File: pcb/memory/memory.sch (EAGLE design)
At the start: 8 parts, among them IC1 CY62256LL-PXC, IC2 CY62256LL-PXC, IC3 74HC04D

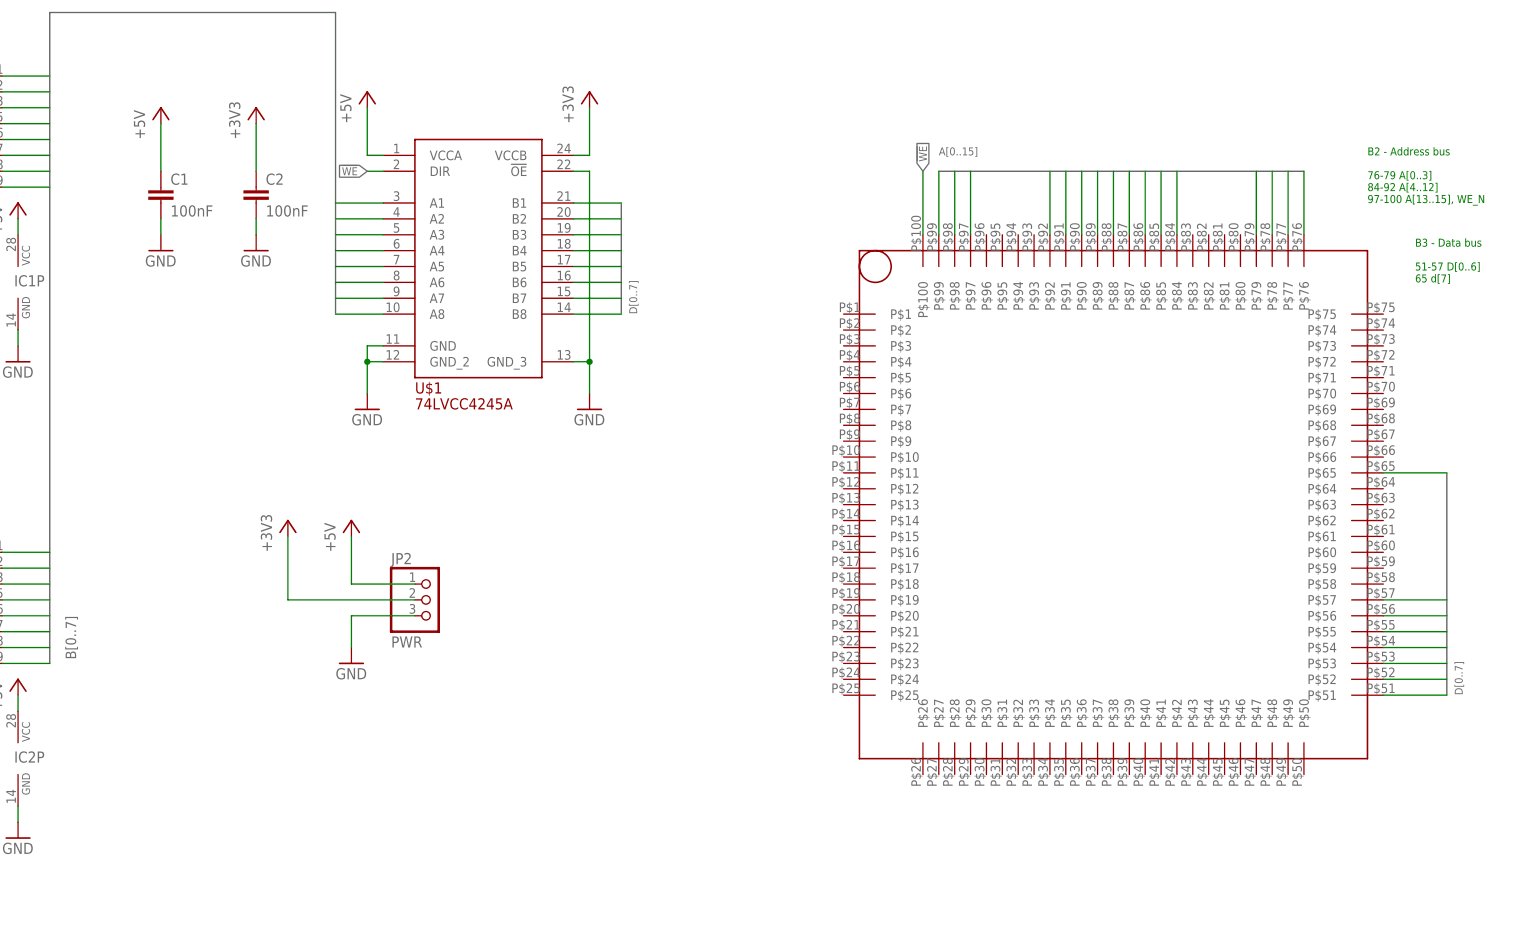
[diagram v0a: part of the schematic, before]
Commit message: Memory board with headers
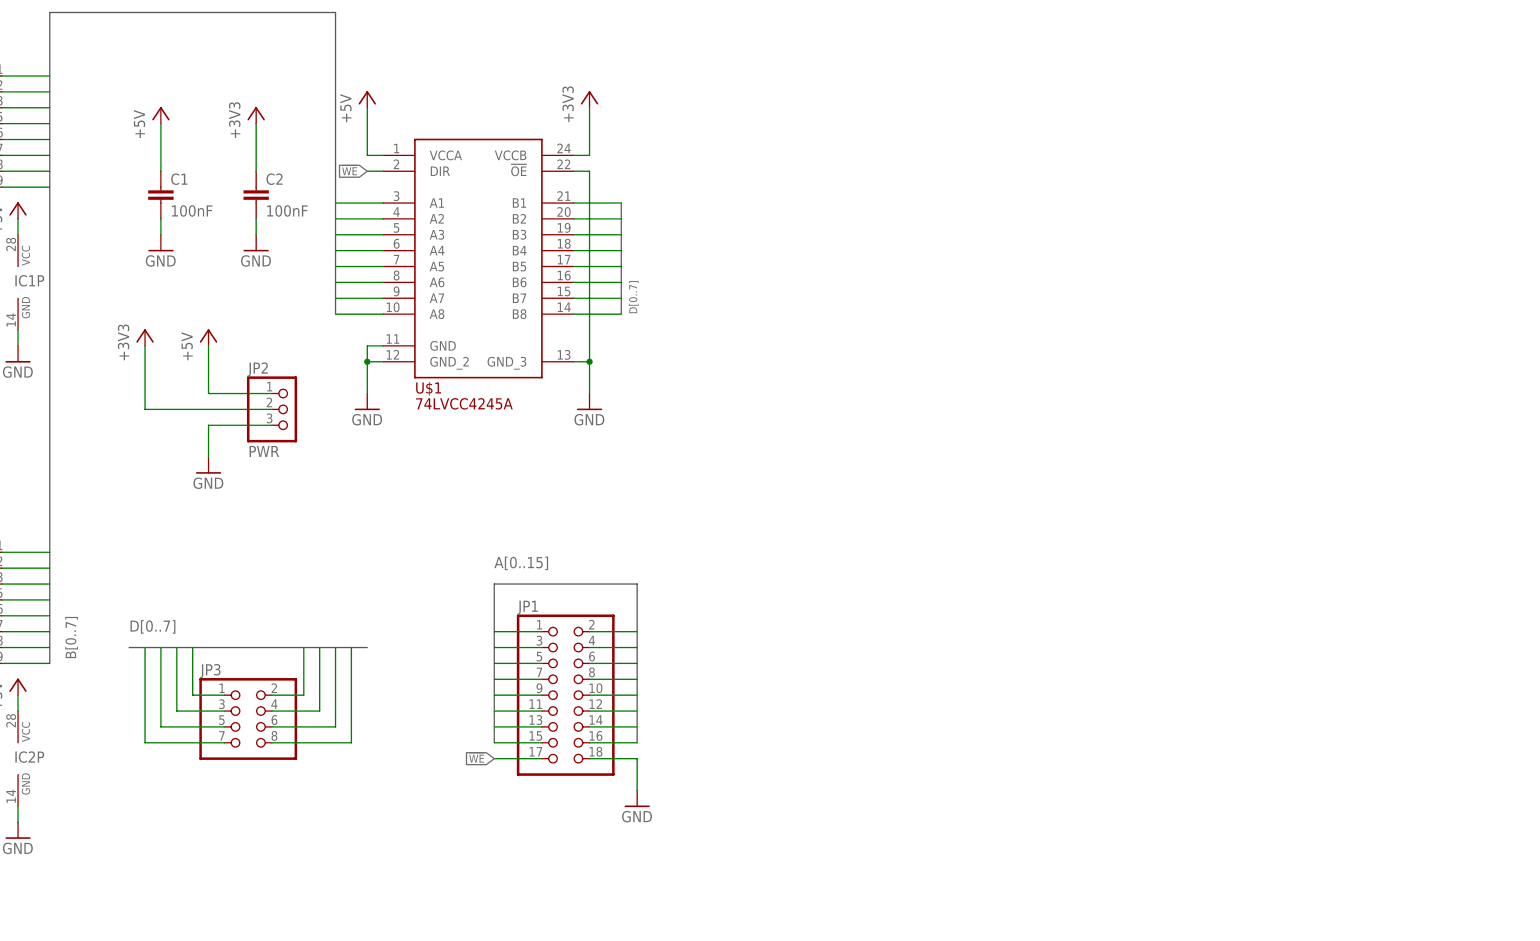
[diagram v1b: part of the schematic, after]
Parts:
- removed U$2: TQFP100_ADAPTER, depmod:TQFP100_ADAPTER
- added JP1: (no value), pinhead:PINHD-2X9
- added JP3: (no value), pinhead:PINHD-2X4
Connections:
- net !WE!: now also JP1.17; no longer U$2.P$100
- net A0: now also JP1.1; no longer U$2.P$76
- net A1: now also JP1.2; no longer U$2.P$77
- net A10: now also JP1.11; no longer U$2.P$90
- net A11: now also JP1.12; no longer U$2.P$91
- net A12: now also JP1.13; no longer U$2.P$92
- net A13: now also JP1.14; no longer U$2.P$97
- net A14: now also JP1.15; no longer U$2.P$98
- net A15: now also JP1.16; no longer U$2.P$99
- net A2: now also JP1.3; no longer U$2.P$78
- net A3: now also JP1.4; no longer U$2.P$79
- net A4: now also JP1.5; no longer U$2.P$84
- net A5: now also JP1.6; no longer U$2.P$85
- net A6: now also JP1.7; no longer U$2.P$86
- net A7: now also JP1.8; no longer U$2.P$87
- net A8: now also JP1.9; no longer U$2.P$88
- net A9: now also JP1.10; no longer U$2.P$89
- net D0: now also JP3.1; no longer U$2.P$51
- net D1: now also JP3.2; no longer U$2.P$52
- net D2: now also JP3.3; no longer U$2.P$53
- net D3: now also JP3.4; no longer U$2.P$54
- net D4: now also JP3.5; no longer U$2.P$55
- net D5: now also JP3.6; no longer U$2.P$56
- net D6: now also JP3.7; no longer U$2.P$57
- net D7: now also JP3.8; no longer U$2.P$65
- net GND: now also JP1.18
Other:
- note removed: "76-79 A[0..3] 84-92 A[4..12] 97-100 A[13..15], WE_N"
- note removed: "B2 - Address bus"
- note removed: "B3 - Data bus 51-57 D[0..6] 65 d[7]"
- moved on the sheet: JP2

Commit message: Single chip sram w/ rom + MCU
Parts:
- removed C1: 100nF, rcl:C-EUC0805
- removed IC3: 74HC04D, 74xx-eu:74HC04D
- removed U$1: 74LCC4245A, depmod:74LCC4245A
- added R1, R2, R3, R4, R5: (no value), rcl:R-EU_M0805
- added S1: SWS004, smd-special:SWS004
- added U1: AS6C1008-55PCN, Alliance_Memory_By_element14_Batch_1:AS6C1008-55PCN
- IC1: value CY62256LL-PXC -> XMEGA16A4A; device memory-sram:CY62256LL-PXC -> atmel:XMEGA16A4A
- IC2: value CY62256LL-PXC -> 24LC256SN; device memory-sram:CY62256LL-PXC -> microchip:24LC256SN
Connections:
- removed net !OE!: IC1G$1.!OE, IC2G$1.!OE, IC3B.O
- removed net B0: IC1G$1.DQ0, IC2G$1.DQ0, U$1.A1
- removed net B1: IC1G$1.DQ1, IC2G$1.DQ1, U$1.A2
- removed net B2: IC1G$1.DQ2, IC2G$1.DQ2, U$1.A3
- removed net B3: IC1G$1.DQ3, IC2G$1.DQ3, U$1.A4
- removed net B4: IC1G$1.DQ4, IC2G$1.DQ4, U$1.A5
- removed net B5: IC1G$1.DQ5, IC2G$1.DQ5, U$1.A6
- removed net B6: IC1G$1.DQ6, IC2G$1.DQ6, U$1.A7
- removed net B7: IC1G$1.DQ7, IC2G$1.DQ7, U$1.A8
- removed net N$1: IC2G$1.!CE, IC3A.O
- new net EE_A0: IC2.A0, R5.1, S1.1
- new net EE_A1: IC2.A1, R4.1, S1.2
- new net EE_A2: IC2.A2, R3.1, S1.3
- new net MEM_RDY: IC1.PB0, JP1.18
- new net SCL: IC1.PE1, IC2.SCL, R2.1
- new net SDA: IC1.PE0, IC2.SDA, R1.1
- net !WE!: now also IC1.PB1, U1.WE; no longer IC1G$1.!WE, IC2G$1.!WE, IC3B.I, U$1.DIR
- net +3V3: now also IC1.VCC, IC1.VCC1, IC1.VCC2, IC2.VCC, R1.2, R2.2, R3.2, R4.2, R5.2, U1.CE2, U1.VCC; no longer U$1.VCCB
- net +5V: no longer C1.1, IC1P.VCC, IC2P.VCC, IC3P.VCC, U$1.VCCA
- net A0: now also IC1.PD0, U1.A0; no longer IC1G$1.A0, IC2G$1.A0
- net A1: now also IC1.PD1, U1.A1; no longer IC1G$1.A1, IC2G$1.A1
- net A10: now also IC1.PC2, IC1.PC3, U1.A10; no longer IC1G$1.A10, IC2G$1.A10
- net A11: now also U1.A11; no longer IC1G$1.A11, IC2G$1.A11
- net A12: now also IC1.PC4, U1.A12; no longer IC1G$1.A12, IC2G$1.A12
- net A13: now also IC1.PC5, U1.A13; no longer IC1G$1.A13, IC2G$1.A13
- net A14: now also IC1.PC6, U1.A14; no longer IC1G$1.A14, IC2G$1.A14
- net A15: now also IC1.PC7, U1.A15; no longer IC1G$1.!CE, IC3A.I
- net A2: now also IC1.PD2, U1.A2; no longer IC1G$1.A2, IC2G$1.A2
- net A3: now also IC1.PD3, U1.A3; no longer IC1G$1.A3, IC2G$1.A3
- net A4: now also IC1.PD4, U1.A4; no longer IC1G$1.A4, IC2G$1.A4
- net A5: now also IC1.PD5, U1.A5; no longer IC1G$1.A5, IC2G$1.A5
- net A6: now also IC1.PD6, U1.A6; no longer IC1G$1.A6, IC2G$1.A6
- net A7: now also IC1.PD7, U1.A7; no longer IC1G$1.A7, IC2G$1.A7
- net A8: now also IC1.PC0, U1.A8; no longer IC1G$1.A8, IC2G$1.A8
- net A9: now also IC1.PC1, U1.A9; no longer IC1G$1.A9, IC2G$1.A9
- net D0: now also IC1.PA0, U1.DQ0; no longer U$1.B1
- net D1: now also IC1.PA1, U1.DQ1; no longer U$1.B2
- net D2: now also IC1.PA2, U1.DQ2; no longer U$1.B3
- net D3: now also IC1.PA3, U1.DQ3; no longer U$1.B4
- net D4: now also IC1.PA4, U1.DQ4; no longer U$1.B5
- net D5: now also IC1.PA5, U1.DQ5; no longer U$1.B6
- net D6: now also IC1.PA6, U1.DQ6; no longer U$1.B7
- net D7: now also IC1.PA7, U1.DQ7; no longer U$1.B8
- net GND: now also IC1.GND, IC1.GND1, IC1.GND2, IC1.GND3, IC2.GND, S1.6, S1.7, S1.8, U1.A16, U1.CE, U1.OE, U1.VSS; no longer C1.2, IC1P.GND, IC2P.GND, IC3P.GND, JP1.18, U$1.!OE!, U$1.GND, U$1.GND_2, U$1.GND_3
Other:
- moved on the sheet: C2, JP1, JP2, JP3

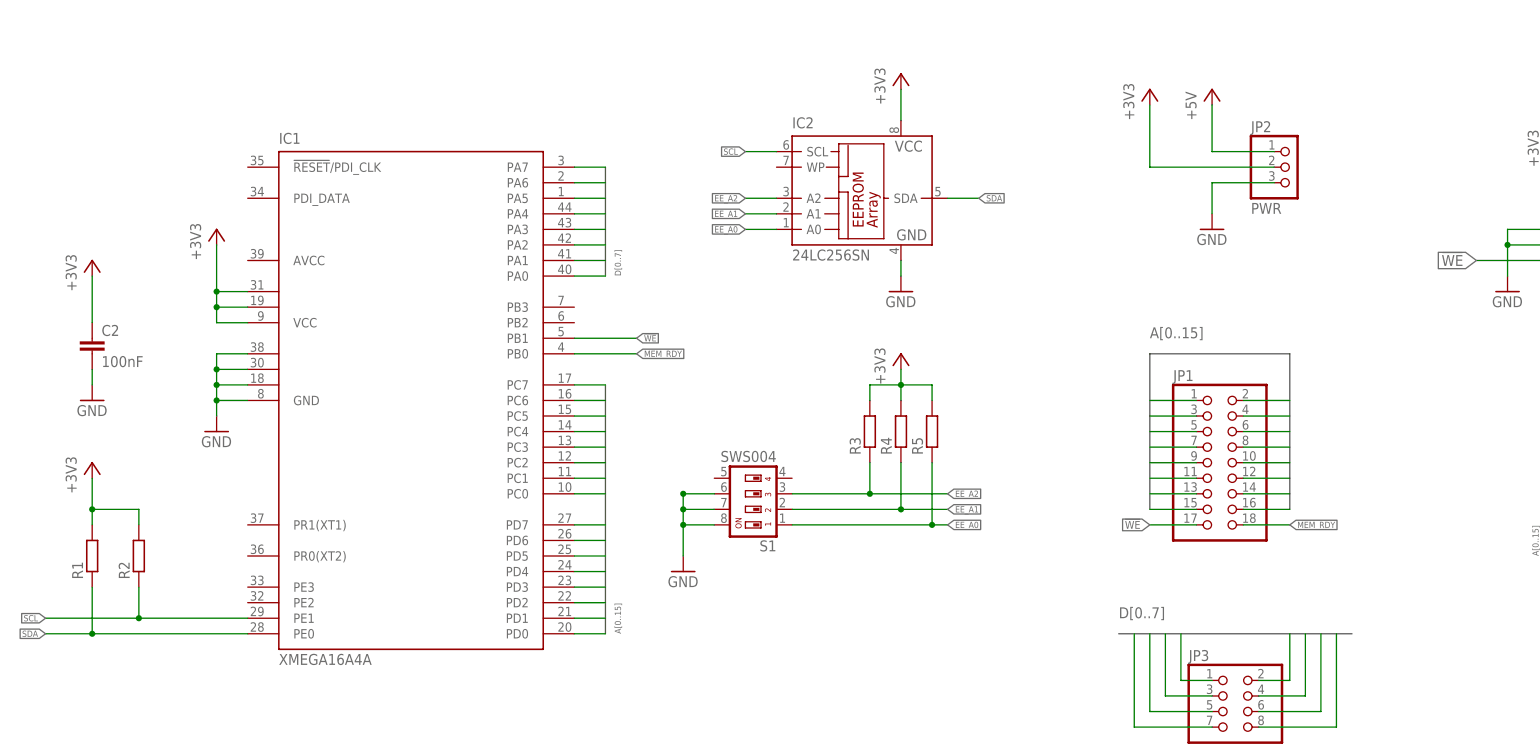
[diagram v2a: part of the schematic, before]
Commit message: Memory board schematic: added leds, isp, reset jumper
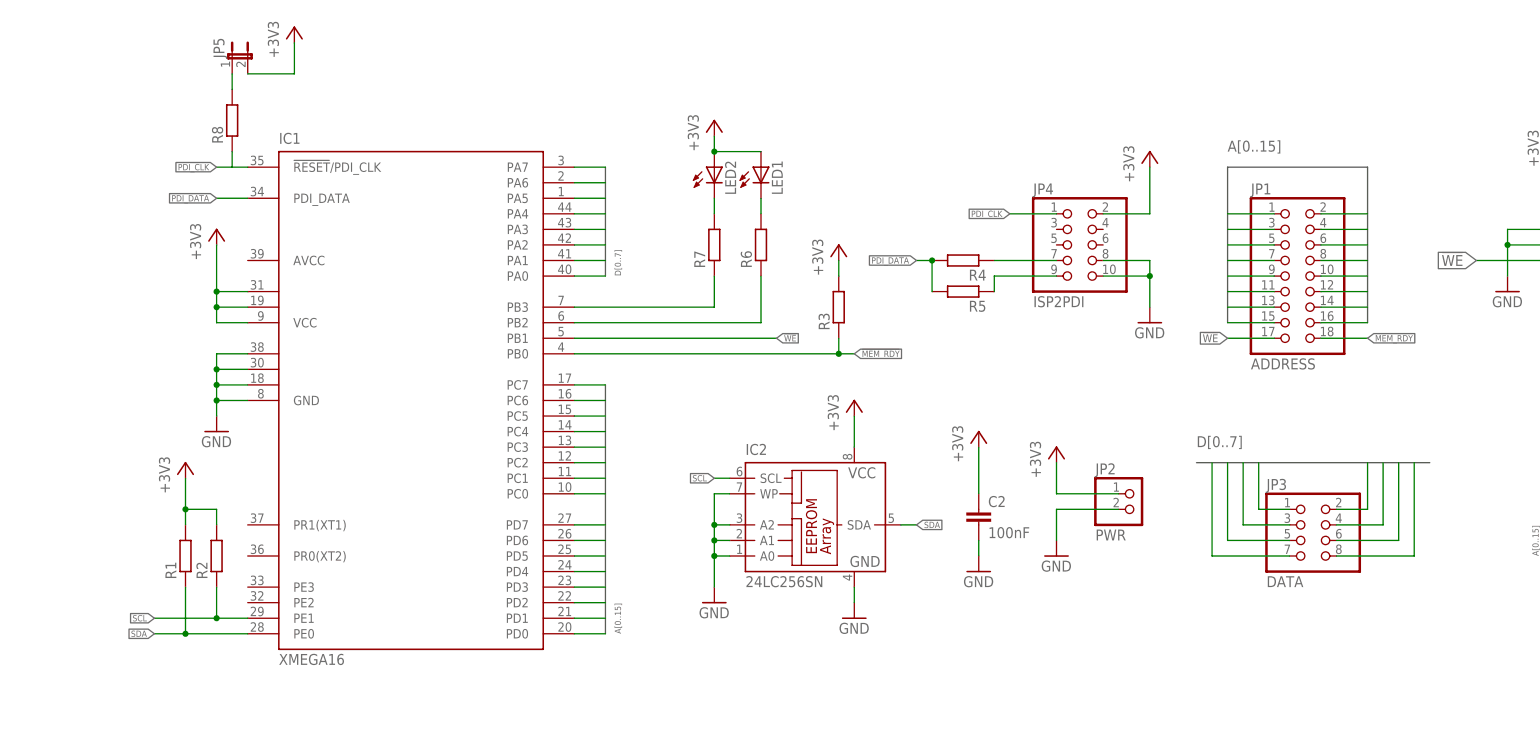
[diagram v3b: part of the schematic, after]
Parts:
- removed S1: SWS004, smd-special:SWS004
- added JP4: ISP2PDI, pinhead:PINHD-2X5
- added JP5: (no value), jumper:JP1E
- added LED1, LED2: (no value), led:LEDSML0805
- added R6, R7, R8: (no value), rcl:R-EU_M0805
- IC1: value XMEGA16A4A -> XMEGA16
- JP1: value (none) -> ADDRESS
- JP2: device pinhead:PINHD-1X3 -> pinhead:PINHD-1X2
- JP3: value (none) -> DATA
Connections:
- removed net +5V: JP2.1
- removed net EE_A0: IC2.A0, R5.1, S1.1
- removed net EE_A1: IC2.A1, R4.1, S1.2
- removed net EE_A2: IC2.A2, R3.1, S1.3
- new net !MEM_RDY!: IC1.PB0, R3.1
- new net N$1: JP4.7, R4.1
- new net N$2: JP4.9, R5.1
- new net N$3: IC1.PB2, R6.1
- new net N$4: IC1.PB3, R7.1
- new net N$5: LED2.C, R7.2
- new net N$6: LED1.C, R6.2
- new net N$7: JP5.1, R8.2
- new net PDI_CLK: IC1.!RESET!/PDI_CLK, JP4.1, R8.1
- new net PDI_DATA: IC1.PDI_DATA, R4.2, R5.2
- net +3V3: now also JP2.1, JP4.2, JP5.2, LED1.A, LED2.A; no longer JP2.2, R4.2, R5.2
- net GND: now also IC2.A0, IC2.A1, IC2.A2, IC2.WP, JP2.2, JP4.10, JP4.8; no longer JP2.3, S1.6, S1.7, S1.8
- net MEM_RDY: no longer IC1.PB0
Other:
- moved on the sheet: C2, IC2, JP1, JP3, R1, R2, R3, R4, R5
